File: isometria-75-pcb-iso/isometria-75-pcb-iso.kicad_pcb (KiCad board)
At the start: 2 copper layers, 308.3 x 123 mm, 314 parts, among them J101 USB, J102 SPI, J103 Conn_01x06_Male, Q101 AO3400A, SW101 RST, SW102 BOOT, SW201 Rotary_Encoder_Switch, U101 XC6206P332MR, U102 STM32F072CBTx, U301 74LVC1G125

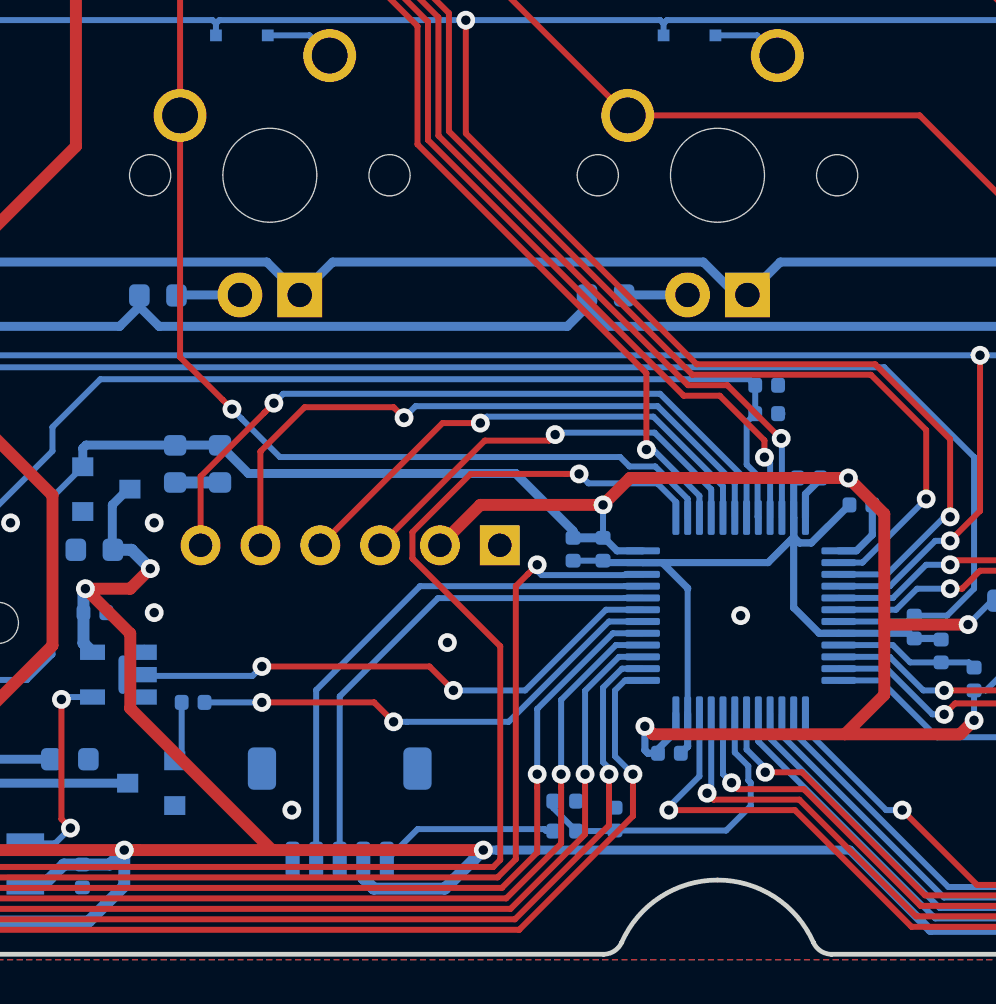
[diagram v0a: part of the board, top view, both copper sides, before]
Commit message: moved underglow from TIM1 to TIM2
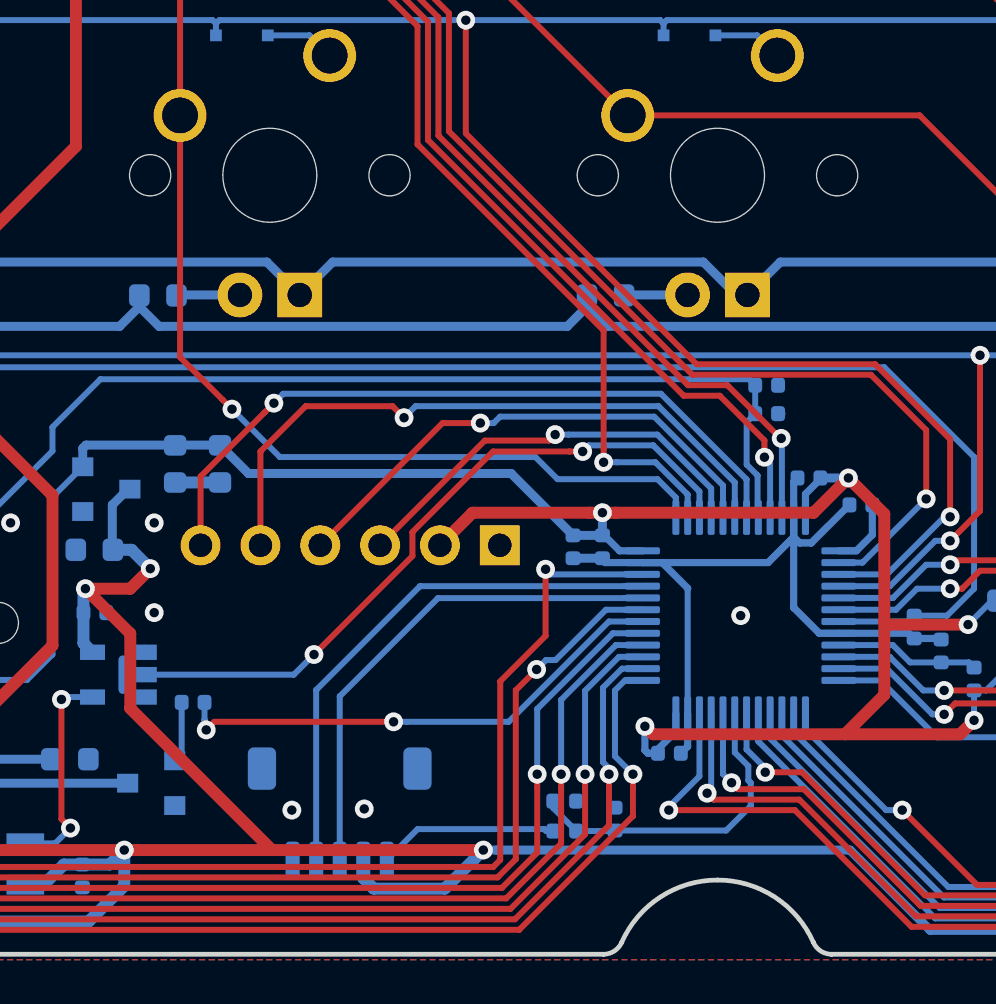
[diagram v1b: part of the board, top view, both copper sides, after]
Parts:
- moved C107 0.11 mm to (151.9, 96.5)
- moved C108 0.10 mm to (150.6, 96.5)
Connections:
- U102 pad 31: UGLED -> COL5
- U102 pad 34: COL5 -> COL6
- U102 pad 37: COL6 -> COL7
- U102 pad 38: COL7 -> ROW0
- U102 pad 39: ROW0 -> UGLED
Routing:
- net COL6: track 186.5 -> 175.1 mm
- net UGLED: track 23.2 -> 30.1 mm
- net COL5: track 167.1 -> 163.4 mm
- net LED_PWM: track 20.7 -> 21.6 mm
- net ROW0: track 423.0 -> 423.9 mm

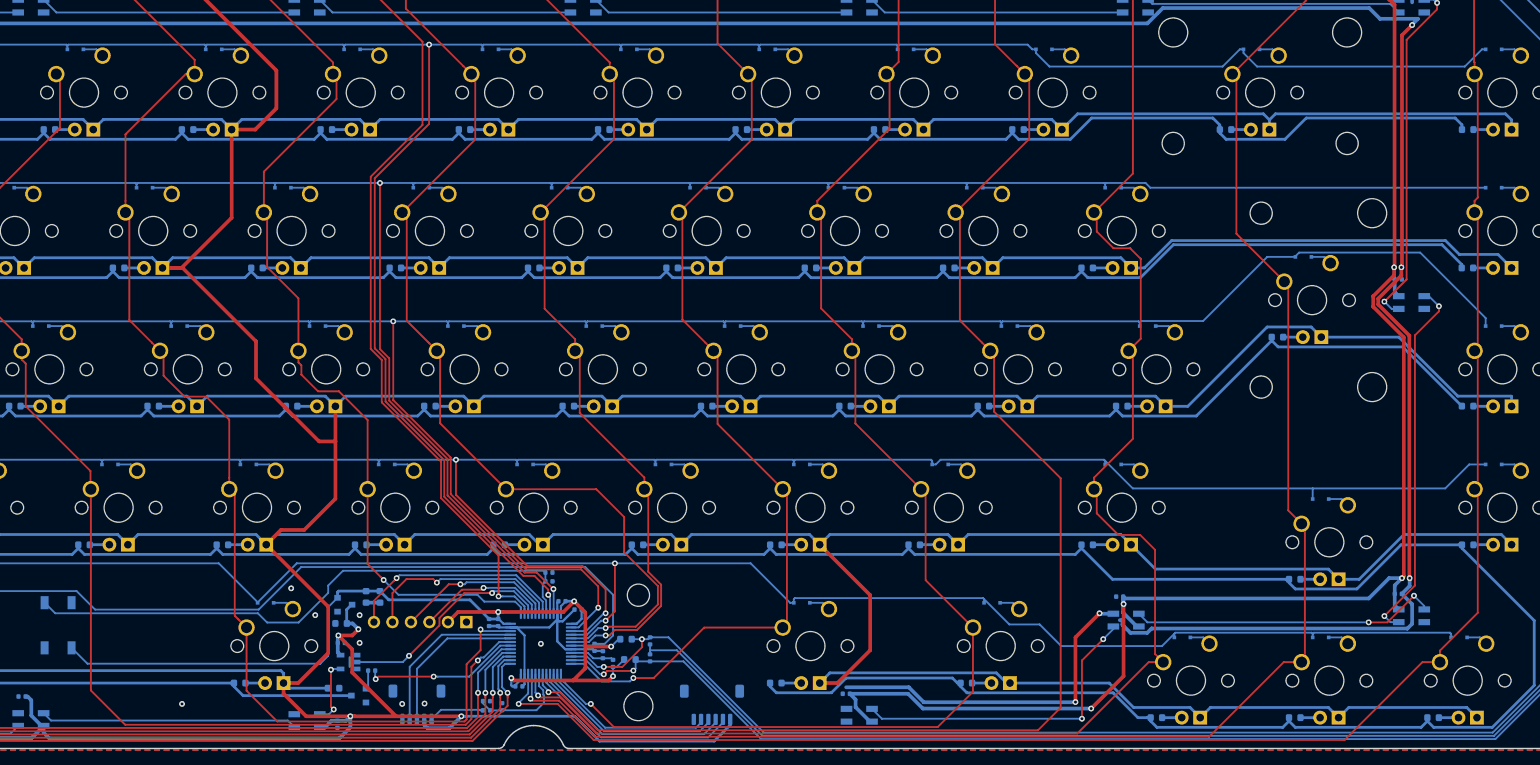
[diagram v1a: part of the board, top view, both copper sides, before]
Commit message: major schematic/pcb rework
rewired SPI, added SPI CS/IRQ/RES pins, rewired part of the matrix in the process
changed to a larger header for SPI
added a divider for input voltage sensing
removed extension header due to a lack of remaining unused GPIOs
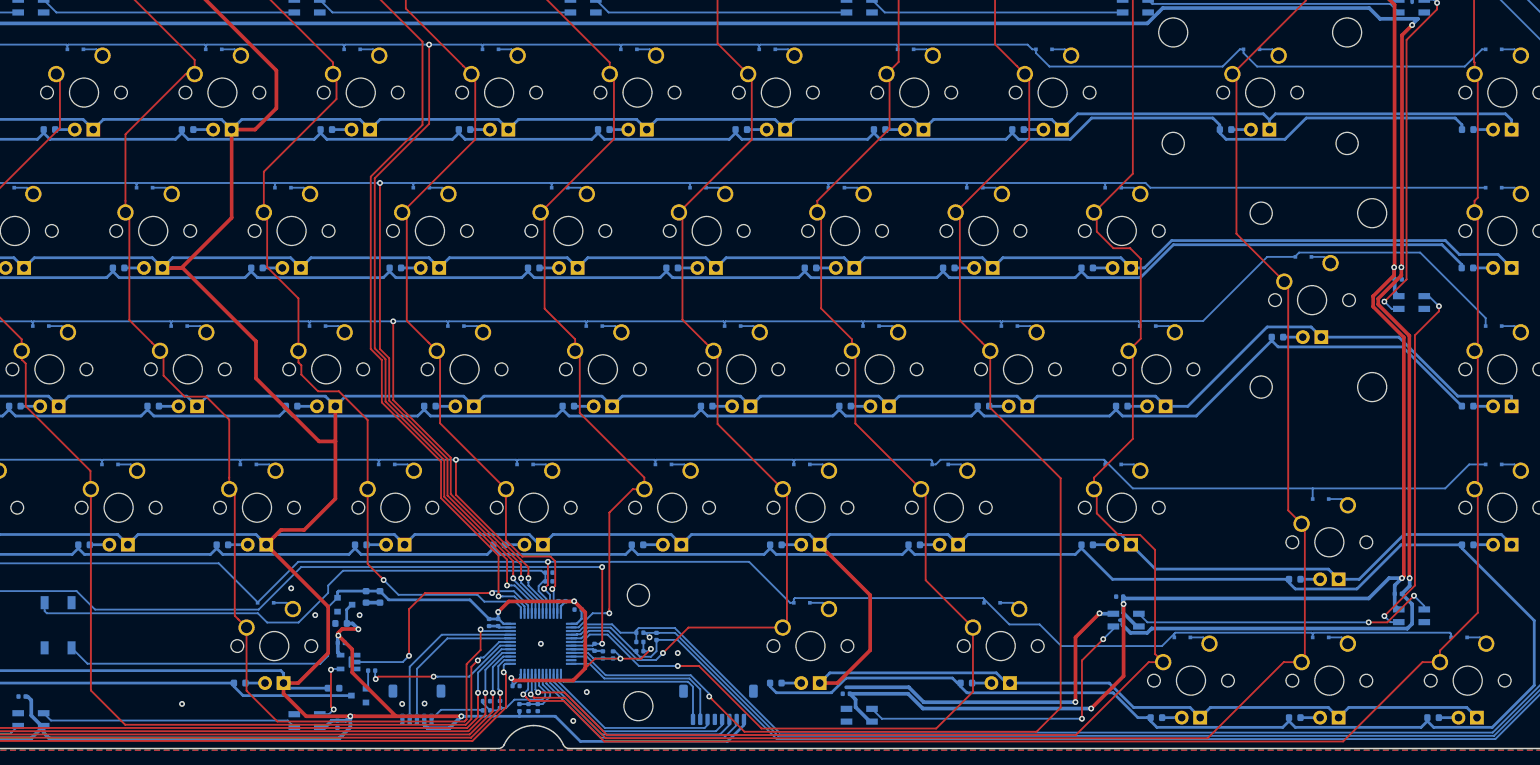
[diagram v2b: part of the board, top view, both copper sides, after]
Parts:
- removed J102: SPI, Connector_JST:JST_SH_SM06B-SRSS-TB_1x06-1MP_P1.00mm_Horizontal
- added C113: 100n, Capacitor_SMD:C_0402_1005Metric, B.Cu at (156.0, 108.2)
- added R104: 50k, Resistor_SMD:R_0402_1005Metric, B.Cu at (154.8, 108.2)
- added R105: 50k, Resistor_SMD:R_0402_1005Metric, B.Cu at (157.3, 108.2)
- J103: value Conn_01x06_Male -> SPI; footprint Connector_PinHeader_2.54mm:PinHeader_1x06_P2.54mm_Vertical -> Connector_JST:JST_SH_SM08B-SRSS-TB_1x08-1MP_P1.00mm_Horizontal
- R283, R284: footprint Resistor_SMD:R_0603_1608Metric -> Resistor_SMD:R_0402_1005Metric
- moved J103 36.4 mm to (182.1, 107.8), turned to 0 degrees
- moved C201 3.08 mm to (173.6, 98.4)
- moved R284 1.94 mm to (171.3, 99.2), turned to 0 degrees
- moved C202 1.79 mm to (171.3, 97.9), turned to 0 degrees
- moved R283 1.79 mm to (171.3, 100.5), turned to 180 degrees
- moved R102 1.17 mm to (167.6, 101.0), turned to 270 degrees
- moved R107 0.42 mm to (152.1, 107.8)
- moved C106 0.38 mm to (154.3, 105.2)
- renumbered C113 to C114, R104 to R106, R105 to R107
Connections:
- net Net-(C110-Pad1) renamed /RST
- net Net-(C111-Pad1) renamed /VDDA
- net Net-(C112-Pad1) renamed /BOOT
- net Net-(C113-Pad1) renamed /sense_charge
- net Vsense renamed chgsense
- J103 pad 1: GND -> SPI_RES
- J103 pad 2: +3V3 -> SPI_IRQ
- J103 pad 3: PB4 -> SPI_CS
- J103 pad 4: PB5 -> GND
- J103 pad 5: PB6_TX1 -> SPI_SCK
- J103 pad 6: PB7_RX1 -> SPI_MISO
- U102 pad 10: ROTB -> COL12
- U102 pad 11: ROTA -> Net-(U102-Pad11)
- U102 pad 12: COL10 -> SPI_IRQ
- U102 pad 13: COL11 -> SPI_RES
- U102 pad 14: SPI_NSS -> SPI_CS
- U102 pad 18: COL12 -> /sense_battV
- U102 pad 2: ROW3 -> COL9
- U102 pad 3: ROW4 -> ROTB
- U102 pad 4: ROW5 -> ROTA
- U102 pad 40: PB4 -> ROW1
- U102 pad 41: PB5 -> ROW2
- U102 pad 42: PB6_TX1 -> ROW3
- U102 pad 43: PB7_RX1 -> ROW4
- U102 pad 45: ROW1 -> ROW5
- U102 pad 46: ROW2 -> COL8
- U102 pad 5: COL8 -> COL10
- U102 pad 6: COL9 -> COL11
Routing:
- net GND: track 841.3 -> 807.7 mm, vias 23 -> 26
- net PB7_RX1: track 30.7 -> 0.00 mm, vias 1 -> 0
- net PB6_TX1: track 28.1 -> 0.00 mm, vias 1 -> 0
- net SPI_CS: track 0.00 -> 25.1 mm
- net SPI_NSS: track 24.0 -> 0.00 mm
- net SPI_RES: track 0.00 -> 23.8 mm
- net SPI_IRQ: track 0.00 -> 23.3 mm
- net COL8: track 140.5 -> 117.3 mm
- net PB5: track 21.9 -> 0.00 mm, vias 1 -> 0
- net PB4: track 18.2 -> 0.00 mm, vias 1 -> 0
- net ROW4: track 339.7 -> 326.0 mm
- net ROW3: track 362.7 -> 350.9 mm
- net /sense_battV: track 0.00 -> 8.15 mm
- net +3V3: track 137.9 -> 130.4 mm
- net ROW5: track 313.8 -> 307.7 mm
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
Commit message: added capacity, rerouted power traces
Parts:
- added C104: 1u, Capacitor_SMD:C_0603_1608Metric, B.Cu at (130.6, 96.9)
- added C105: 4.7u, Capacitor_SMD:C_0603_1608Metric, B.Cu at (131.3, 110.5)
- added C106: 1u, Capacitor_SMD:C_0603_1608Metric, B.Cu at (133.7, 93.0)
- C101: value 1u -> 100u; footprint Capacitor_SMD:C_0603_1608Metric -> Capacitor_Tantalum_SMD:CP_EIA-3528-21_Kemet-B
- C102: value 4.7u -> 100u; footprint Capacitor_SMD:C_0603_1608Metric -> Capacitor_Tantalum_SMD:CP_EIA-3528-21_Kemet-B
- C103: value 1u -> 10u; footprint Capacitor_SMD:C_0603_1608Metric -> Capacitor_Tantalum_SMD:CP_EIA-3216-18_Kemet-A
- moved C103 13.8 mm to (131.0, 106.5), turned to 90 degrees
- moved R101 11.8 mm to (146.3, 102.7)
- moved C101 10.5 mm to (134.2, 106.4), turned to 90 degrees
- moved C102 9.83 mm to (134.7, 97.3), turned to 90 degrees
- moved Q101 6.01 mm to (126.7, 105.9)
- moved C302 0.33 mm to (129.5, 110.4), turned to 90 degrees
- turned U101 to 90 degrees
- renumbered C104 to C107, C105 to C108, C106 to C109, C107 to C110, C108 to C111, C109 to C112, C110 to C113, C111 to C114, C112 to C115, C113 to C116, C114 to C117, J103 to J102
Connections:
- C103 pad 1: +3V3 -> +5V
- J102 pad 8: +5V -> +3V3
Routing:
- net +5V: track 2752.5 -> 2694.1 mm, vias 14 -> 12
- net +3V3: track 130.4 -> 158.9 mm
- net Net-(Q101-Pad1): track 2.60 -> 20.5 mm, vias 0 -> 2
- net LED_PWM: track 21.6 -> 8.00 mm, vias 2 -> 0
- net GND: track 807.7 -> 802.3 mm
- net LED-: track 1898.3 -> 1894.4 mm
- net /RST: track 107.1 -> 103.4 mm
- net UGLED: track 33.3 -> 29.6 mm
- net Net-(D301-Pad3): track 9.16 -> 10.7 mm
- net /BOOT: track 80.8 -> 82.3 mm
- net Net-(D304-Pad1): track 63.2 -> 63.9 mm
- net SPI_CS: track 25.1 -> 25.8 mm
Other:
- net class Power: trace_width 0.381 -> 0.508

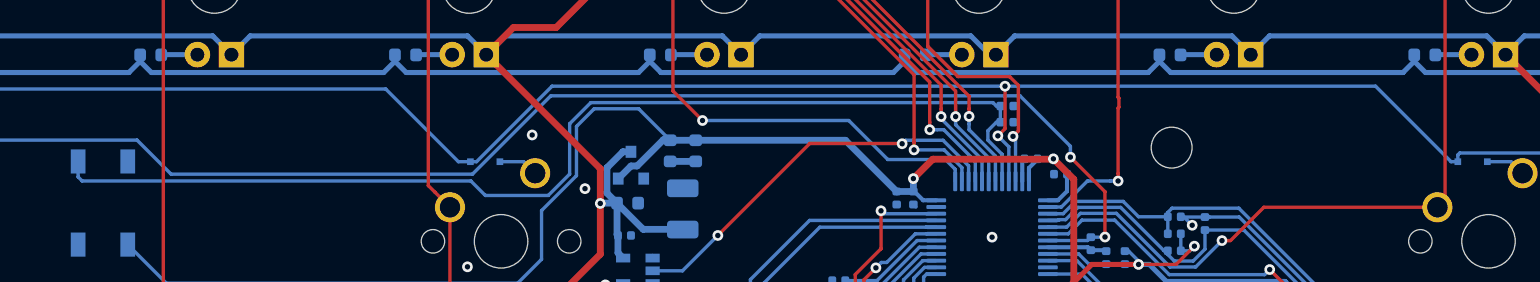
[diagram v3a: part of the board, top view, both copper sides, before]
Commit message: cosmetic silkscreen fixes
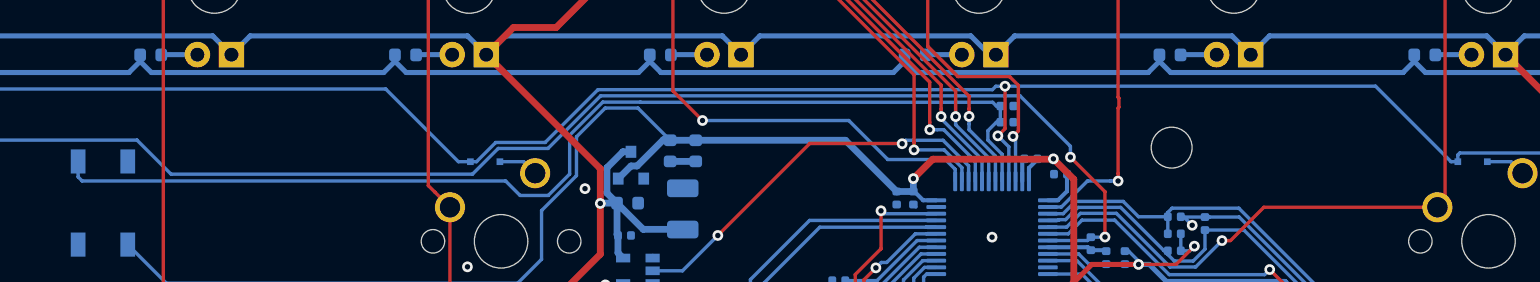
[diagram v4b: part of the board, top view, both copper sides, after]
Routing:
- net GND: vias 26 -> 25

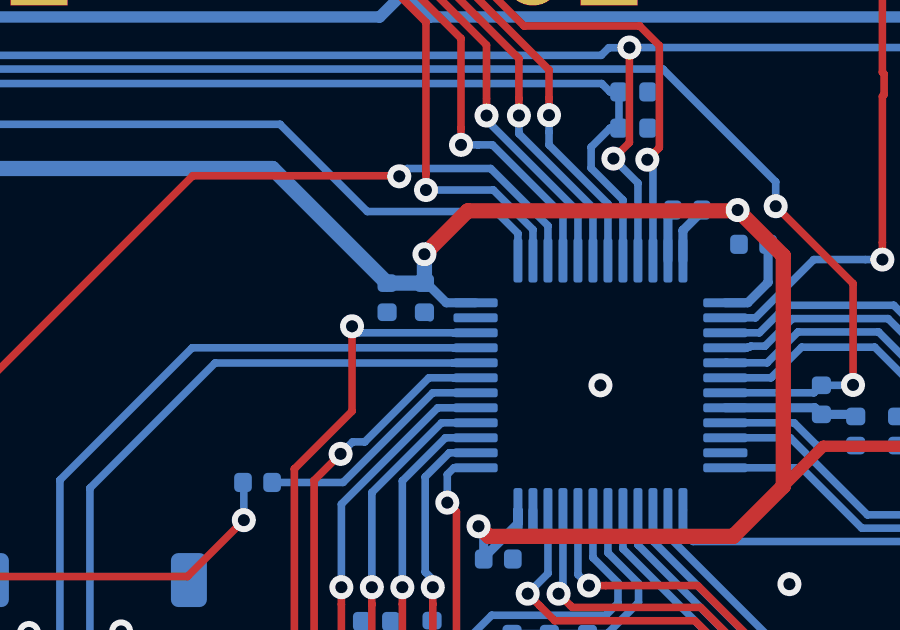
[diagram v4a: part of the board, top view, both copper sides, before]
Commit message: fixed a groundplane error
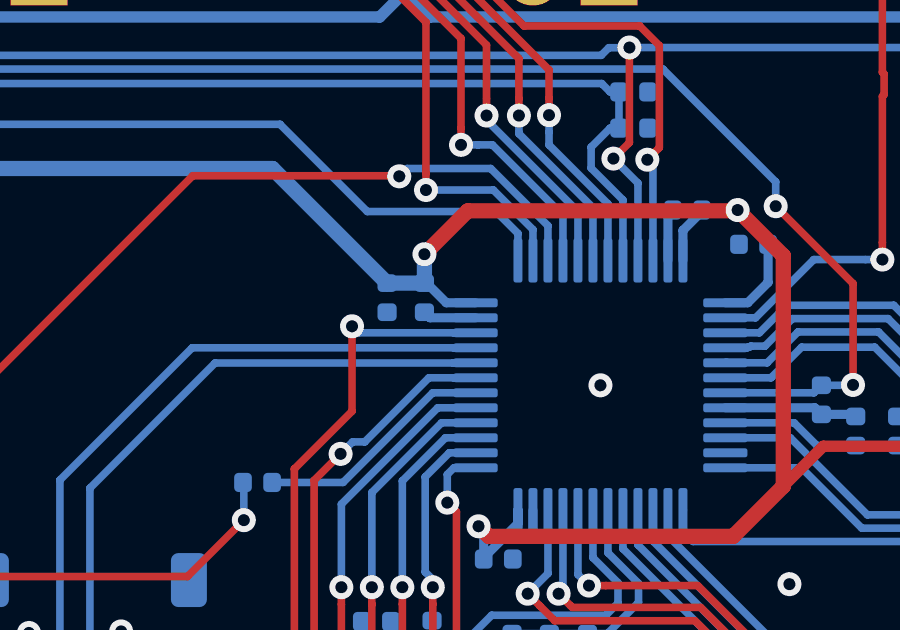
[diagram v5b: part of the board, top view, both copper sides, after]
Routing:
- net GND: track 802.3 -> 804.1 mm
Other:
- net class Power: trace_width 0.508 -> 0.3048
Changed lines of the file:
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@@
     (thickness 1.6)
     (drawings 37)
-    (tracks 2431)
+    (tracks 2433)
     (zones 0)
     (modules 319)
@@
   (net_class Power ""
     (clearance 0.1905)
-    (trace_width 0.508)
+    (trace_width 0.3048)
     (via_dia 0.8)
     (via_drill 0.4)
@@
   (via (at 18.796 107.696) (size 0.8) (drill 0.4) (layers F.Cu B.Cu) (net 1))
   (via (at -4.826 107.696) (size 0.8) (drill 0.4) (layers F.Cu B.Cu) (net 1))
-  (via (at 157.734 99.441) (size 0.8) (drill 0.4) (layers F.Cu B.Cu) (net 1))
   (via (at 141.7574 107.6452) (size 0.8) (drill 0.4) (layers F.Cu B.Cu) (net 1))
   (via (at 162.179 110.0328) (size 0.8) (drill 0.4) (layers F.Cu B.Cu) (net 1))
@@
   (segment (start 131.3435 97.0025) (end 131.3435 96.901) (width 0.508) (layer B.Cu) (net 1))
   (via (at 118.618 101.6508) (size 0.8) (drill 0.4) (layers F.Cu B.Cu) (net 1))
+  (segment (start 152.0526 97.191) (end 151.8666 97.005) (width 0.3048) (layer B.Cu) (net 1))
+  (segment (start 153.5715 97.191) (end 152.0526 97.191) (width 0.3048) (layer B.Cu) (net 1))
+  (via (at 157.734 99.441) (size 0.8) (drill 0.4) (layers F.Cu B.Cu) (net 1))
   (segment (start 135.636 92.2145) (end 133.731 92.2145) (width 0.508) (layer B.Cu) (net 2))
   (segment (start 146.8015 92.2145) (end 150.622 96.035) (width 0.508) (layer B.Cu) (net 2))
@@
   (segment (start 131.515022 89.369889) (end 131.527733 89.3826) (width 0.254) (layer B.Cu) (net 229))
   (segment (start 131.527733 89.3826) (end 157.7771 89.3826) (width 0.254) (layer B.Cu) (net 229))
-  (zone (net 1) (net_name GND) (layer B.Cu) (hatch edge 0.508)
-    (connect_pads (clearance 0.2032))
-    (min_thickness 0.1905)
-    (fill yes (arc_segments 32) (thermal_gap 0.1905) (thermal_bridge_width 0.508) (smoothing chamfer) (radius 0.2))
-    (polygon
-      (pts
-        (xy 299.212 114.046) (xy -9.525 114.046) (xy -9.525 -9.525) (xy 299.212 -9.525)
-      )
-    )
-  )
   (zone (net 1) (net_name GND) (layer F.Cu) (hatch edge 0.508)
     (connect_pads (clearance 0.2032))
@@
       )
     )
+  )
+  (zone (net 1) (net_name GND) (layer B.Cu) (hatch edge 0.508)
+    (connect_pads (clearance 0.2032))
+    (min_thickness 0.1905)
+    (fill yes (arc_segments 32) (thermal_gap 0.1905) (thermal_bridge_width 0.508) (smoothing chamfer) (radius 0.2))
+    (polygon
+      (pts
+        (xy 299.212 114.046) (xy -9.525 114.046) (xy -9.525 -9.525) (xy 299.212 -9.525)
+      )
+    )
